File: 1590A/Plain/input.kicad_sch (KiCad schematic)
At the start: 13 parts, among them Q201 MMBF5103, Q202 BC857C

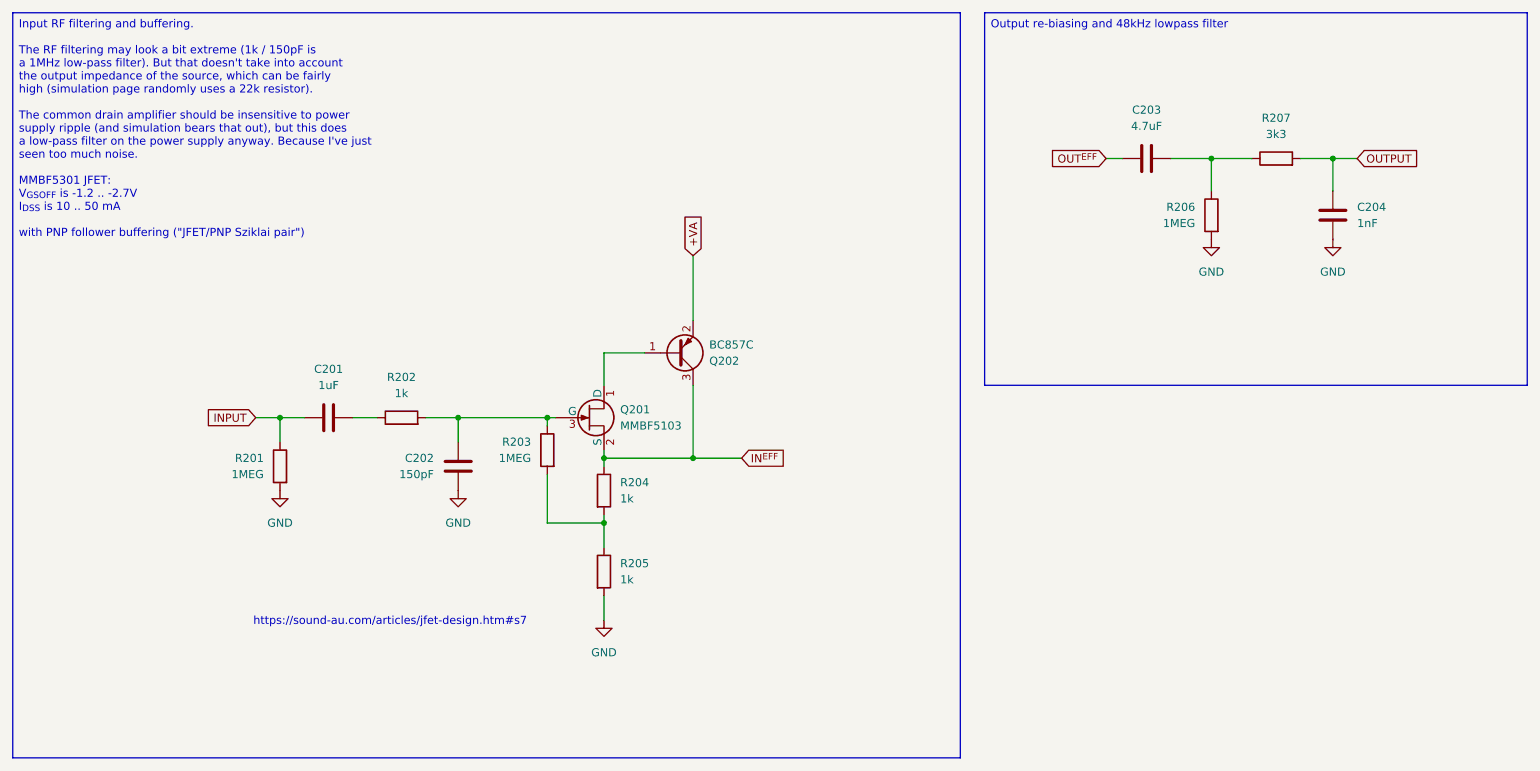
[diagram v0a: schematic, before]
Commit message: Update plain 1590A board
I had decided that the effect board didn't need the input to be
ground-biased, and that was very wrong, and made some of my old effect
boards not work.  So add the AC couple capacitor and resistor to ground.

Also do the same boring RC power smoothing with the voodoo ferrite for
the +VA line.  Let's keep it simple and realistic - the noise isn't some
60Hz ripple, it's all SMPS high-frequency stuff.

Signed-off-by: Linus Torvalds <torvalds@linux-foundation.org>
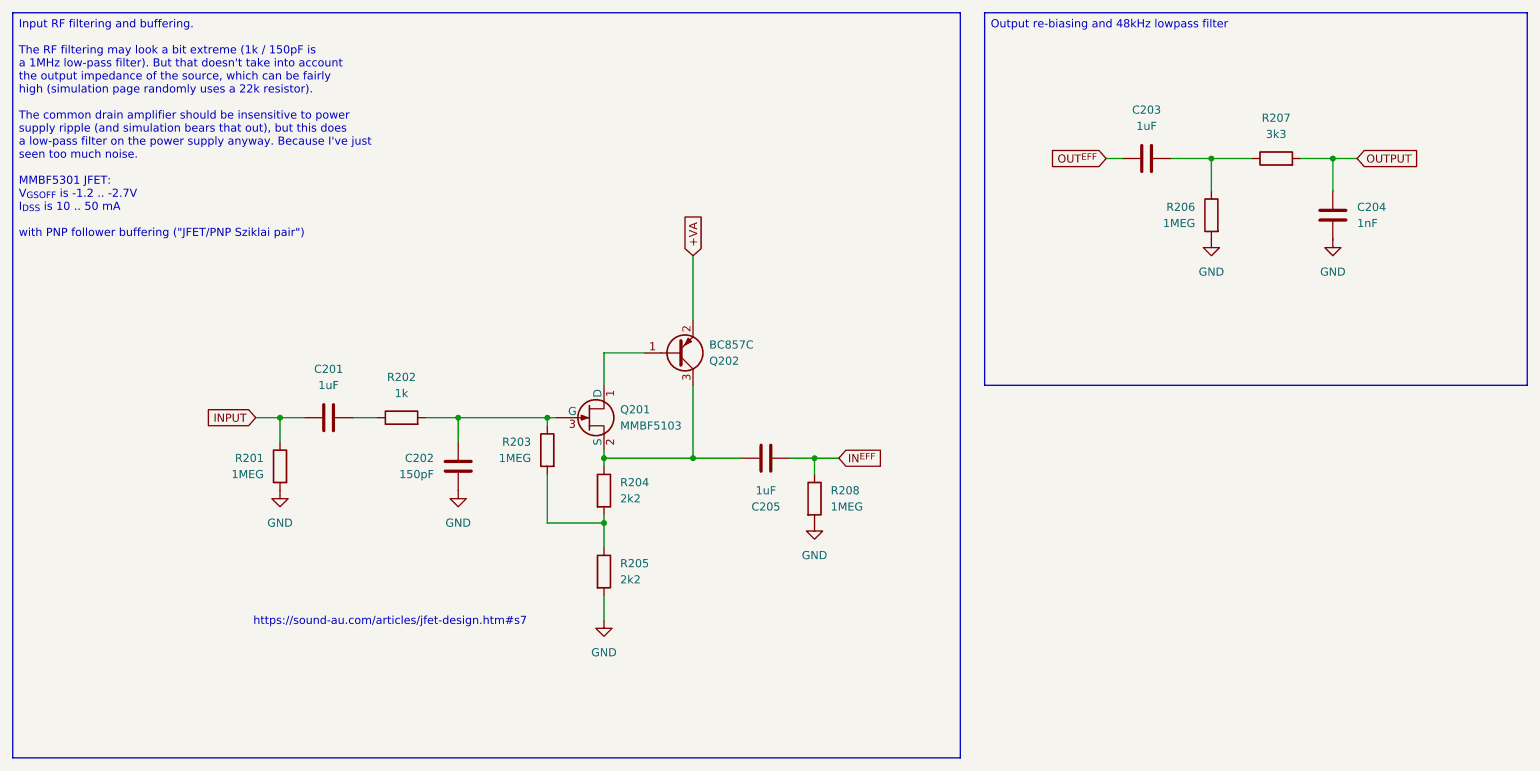
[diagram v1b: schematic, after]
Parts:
- added C205: 1uF, Capacitor_SMD:C_1206_3216Metric, symbol Device:C
- added R208: 1MEG, Resistor_SMD:R_0805_2012Metric, symbol Device:R
- C203: value 4.7uF -> 1uF
- R204, R205: value 1k -> 2k2
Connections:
- net GND: now also R208.2
- net IN^{EFF}: now also C205.2, R208.1; no longer Q201.2 (S), Q202.3 (C), R204.1
- new net: C205.1, Q201.2 (S), Q202.3 (C), R204.1
